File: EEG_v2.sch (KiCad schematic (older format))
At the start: 5 parts, among them P1 CONN_5, P2 CONN_1, P3 CONN_1, P4 USB_A, SW1 SPST

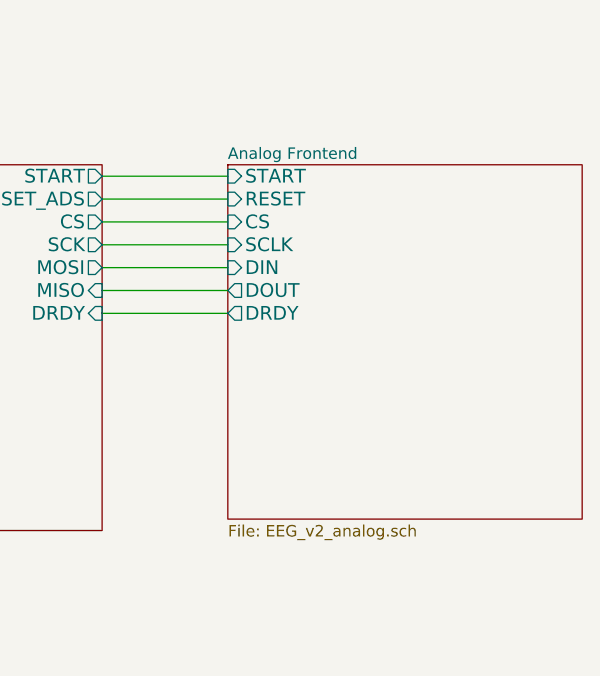
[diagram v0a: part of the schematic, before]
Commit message: Imported sheet pins to main sheet
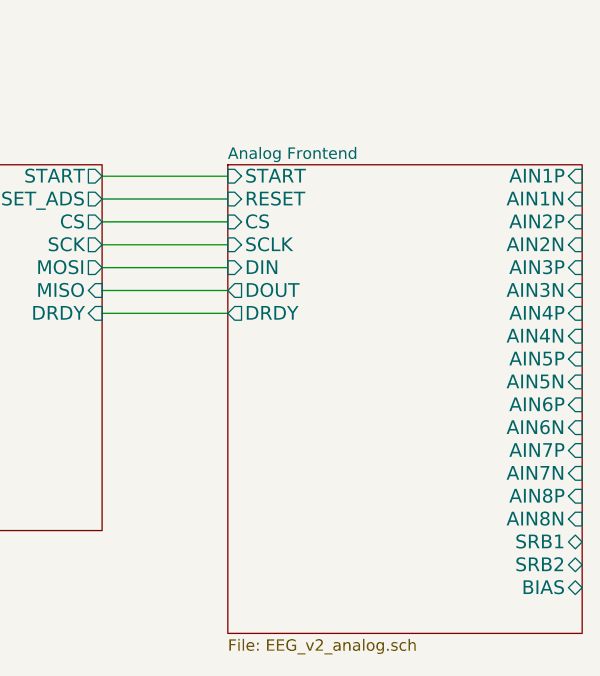
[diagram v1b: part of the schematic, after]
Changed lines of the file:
@@
 $EndDescr
 $Sheet
-S 7000 4200 1550 1550
+S 7000 4200 1550 2050
 U 54B45B18
 F0 "Analog Frontend" 50
@@
 F7 "DOUT" O L 7000 4750 60
 F8 "DRDY" O L 7000 4850 60
+F9 "AIN1P" I R 8550 4250 60
+F10 "AIN1N" I R 8550 4350 60
+F11 "AIN2P" I R 8550 4450 60
+F12 "AIN2N" I R 8550 4550 60
+F13 "AIN3P" I R 8550 4650 60
+F14 "AIN3N" I R 8550 4750 60
+F15 "AIN4P" I R 8550 4850 60
+F16 "AIN4N" I R 8550 4950 60
+F17 "AIN5P" I R 8550 5050 60
+F18 "AIN5N" I R 8550 5150 60
+F19 "AIN6P" I R 8550 5250 60
+F20 "AIN6N" I R 8550 5350 60
+F21 "AIN7P" I R 8550 5450 60
+F22 "AIN7N" I R 8550 5550 60
+F23 "AIN8P" I R 8550 5650 60
+F24 "AIN8N" I R 8550 5750 60
+F25 "SRB1" B R 8550 5850 60
+F26 "SRB2" B R 8550 5950 60
+F27 "BIAS" B R 8550 6050 60
 $EndSheet
 $Sheet

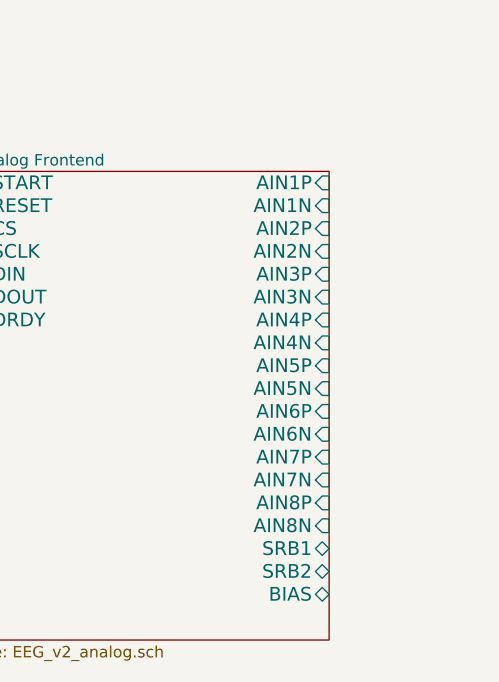
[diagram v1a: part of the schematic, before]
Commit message: Add pin headers for electrodes and debug signals.
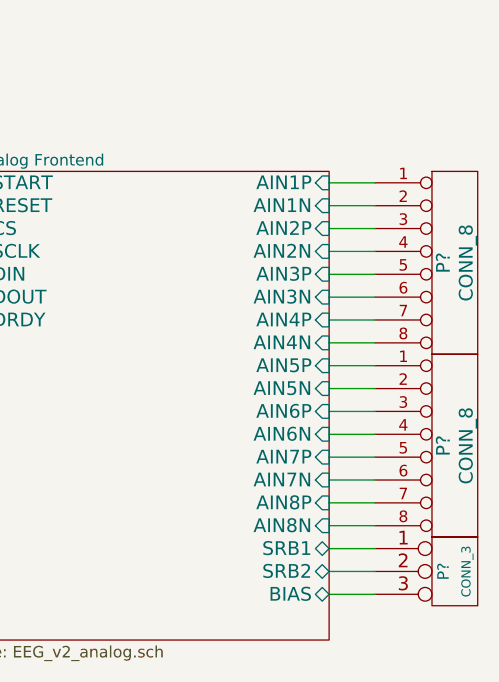
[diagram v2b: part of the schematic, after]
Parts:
- added P? (x2): CONN_8, ~, symbol CONN_8
- added P?: CONN_3, ~, symbol CONN_3
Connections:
- wire segments 26 -> 45
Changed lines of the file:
@@
 Text Notes 1950 6250 0    60   ~ 0
 Note: May change to VIN_RAW instead. Will test first.
+$Comp
+L CONN_8 P?
+U 1 1 54C84F21
+P 9100 4600
+F 0 "P?" V 9050 4600 60  0000 C CNN
+F 1 "CONN_8" V 9150 4600 60  0000 C CNN
+F 2 "~" H 9100 4600 60  0000 C CNN
+F 3 "~" H 9100 4600 60  0000 C CNN
+	1    9100 4600
+	1    0    0    -1
+$EndComp
+$Comp
+L CONN_8 P?
+U 1 1 54C84F2E
+P 9100 5400
+F 0 "P?" V 9050 5400 60  0000 C CNN
+F 1 "CONN_8" V 9150 5400 60  0000 C CNN
+F 2 "~" H 9100 5400 60  0000 C CNN
+F 3 "~" H 9100 5400 60  0000 C CNN
+	1    9100 5400
+	1    0    0    -1
+$EndComp
+$Comp
+L CONN_3 P?
+U 1 1 54C84FBA
+P 9100 5950
+F 0 "P?" V 9050 5950 50  0000 C CNN
+F 1 "CONN_3" V 9150 5950 40  0000 C CNN
+F 2 "~" H 9100 5950 60  0000 C CNN
+F 3 "~" H 9100 5950 60  0000 C CNN
+	1    9100 5950
+	1    0    0    -1
+$EndComp
+Wire Wire Line
+	8550 4250 8750 4250
+Wire Wire Line
+	8750 4350 8550 4350
+Wire Wire Line
+	8550 4450 8750 4450
+Wire Wire Line
+	8750 4550 8550 4550
+Wire Wire Line
+	8550 4650 8750 4650
+Wire Wire Line
+	8750 4750 8550 4750
+Wire Wire Line
+	8550 4850 8750 4850
+Wire Wire Line
+	8750 4950 8550 4950
+Wire Wire Line
+	8550 5050 8750 5050
+Wire Wire Line
+	8750 5150 8550 5150
+Wire Wire Line
+	8550 5250 8750 5250
+Wire Wire Line
+	8750 5350 8550 5350
+Wire Wire Line
+	8550 5450 8750 5450
+Wire Wire Line
+	8750 5550 8550 5550
+Wire Wire Line
+	8550 5650 8750 5650
+Wire Wire Line
+	8750 5750 8550 5750
+Wire Wire Line
+	8550 5850 8750 5850
+Wire Wire Line
+	8750 5950 8550 5950
+Wire Wire Line
+	8550 6050 8750 6050
 $EndSCHEMATC

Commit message: Correct pin headers
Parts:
- removed P1: CONN_5, ~, symbol CONN_5
- added P?: CONN_5X2, ~, symbol CONN_5X2
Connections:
- wire segments 45 -> 54
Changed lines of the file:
@@
 	2650 4750 2750 4750
-Wire Wire Line
-	2750 4750 2750 5400
 Wire Wire Line
 	2650 4850 2750 4850
 Connection ~ 2750 4850
 Wire Wire Line
-	2650 4950 2750 4950
+	2750 4950 2650 4950
 Connection ~ 2750 4950
 $Comp
 L AGND #PWR01
 U 1 1 54C3BF39
-P 3100 5100
-F 0 "#PWR01" H 3100 5100 40  0001 C CNN
-F 1 "AGND" H 3100 5030 50  0000 C CNN
-F 2 "~" H 3100 5100 60  0000 C CNN
-F 3 "~" H 3100 5100 60  0000 C CNN
-	1    3100 5100
-	0    -1   -1   0
+P 2750 5050
+F 0 "#PWR01" H 2750 5050 40  0001 C CNN
+F 1 "AGND" H 2750 4980 50  0000 C CNN
+F 2 "~" H 2750 5050 60  0000 C CNN
+F 3 "~" H 2750 5050 60  0000 C CNN
+	1    2750 5050
+	1    0    0    -1
 $EndComp
 $Comp
@@
 Text Notes 2550 3250 0    60   ~ 0
 BATT_-
-$Comp
-L CONN_5 P1
-U 1 1 54C4DEF5
-P 2200 5600
-F 0 "P1" V 2150 5600 50  0000 C CNN
-F 1 "CONN_5" V 2250 5600 50  0000 C CNN
-F 2 "~" H 2200 5600 60  0000 C CNN
-F 3 "~" H 2200 5600 60  0000 C CNN
-	1    2200 5600
-	-1   0    0    1
-$EndComp
-Wire Wire Line
-	2750 5400 2600 5400
-Wire Wire Line
-	2750 5100 3100 5100
-Connection ~ 2750 5100
-Wire Wire Line
-	2600 5500 4900 5500
-Wire Wire Line
-	2600 5600 4900 5600
-Wire Wire Line
-	4900 5700 2600 5700
-Wire Wire Line
-	2600 5800 2750 5800
-Wire Wire Line
-	2750 5800 2750 6000
+Wire Wire Line
+	2550 5600 4900 5600
+Wire Wire Line
+	4900 5700 3650 5700
 $Comp
 L +3.3V #PWR03
 U 1 1 54C4F12C
-P 2750 6000
-F 0 "#PWR03" H 2750 5960 30  0001 C CNN
-F 1 "+3.3V" H 2750 6110 30  0000 C CNN
-F 2 "~" H 2750 6000 60  0000 C CNN
-F 3 "~" H 2750 6000 60  0000 C CNN
-	1    2750 6000
-	-1   0    0    1
+P 2650 5350
+F 0 "#PWR03" H 2650 5310 30  0001 C CNN
+F 1 "+3.3V" H 2650 5460 30  0000 C CNN
+F 2 "~" H 2650 5350 60  0000 C CNN
+F 3 "~" H 2650 5350 60  0000 C CNN
+	1    2650 5350
+	1    0    0    -1
 $EndComp
 Text Notes 1950 6250 0    60   ~ 0
@@
 Wire Wire Line
 	8550 6050 8750 6050
+$Comp
+L CONN_5X2 P?
+U 1 1 54C8BF12
+P 2150 5700
+F 0 "P?" H 2150 6000 60  0000 C CNN
+F 1 "CONN_5X2" V 2150 5700 50  0000 C CNN
+F 2 "~" H 2150 5700 60  0000 C CNN
+F 3 "~" H 2150 5700 60  0000 C CNN
+	1    2150 5700
+	1    0    0    -1
+$EndComp
+Wire Wire Line
+	2750 4750 2750 5050
+$Comp
+L AGND #PWR?
+U 1 1 54C8DF7C
+P 1450 5500
+F 0 "#PWR?" H 1450 5500 40  0001 C CNN
+F 1 "AGND" H 1450 5430 50  0000 C CNN
+F 2 "~" H 1450 5500 60  0000 C CNN
+F 3 "~" H 1450 5500 60  0000 C CNN
+	1    1450 5500
+	0    1    1    0
+$EndComp
+Wire Wire Line
+	1650 5550 3650 5550
+Wire Wire Line
+	1650 5550 1650 5600
+Wire Wire Line
+	1650 5600 1750 5600
+Wire Wire Line
+	3650 5550 3650 5500
+Wire Wire Line
+	3650 5500 4900 5500
+Wire Wire Line
+	2550 5500 2650 5500
+Wire Wire Line
+	2650 5500 2650 5350
+Wire Wire Line
+	1750 5500 1450 5500
+Wire Wire Line
+	3650 5700 3650 5750
+Wire Wire Line
+	3650 5750 1650 5750
+Wire Wire Line
+	1650 5750 1650 5800
+Wire Wire Line
+	1650 5800 1750 5800
+$Comp
+L +3.3V #PWR?
+U 1 1 54C95C9F
+P 1400 5850
+F 0 "#PWR?" H 1400 5810 30  0001 C CNN
+F 1 "+3.3V" H 1400 5960 30  0000 C CNN
+F 2 "~" H 1400 5850 60  0000 C CNN
+F 3 "~" H 1400 5850 60  0000 C CNN
+	1    1400 5850
+	1    0    0    -1
+$EndComp
+Wire Wire Line
+	1750 5900 1400 5900
+Wire Wire Line
+	1400 5900 1400 5850
 $EndSCHEMATC

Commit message: Modify libraries to be correct. Add pushbuttons and LEDs. Change switch to toggle.
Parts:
- removed SW1: SPST, ~, symbol SPST
- added SW1: SWITCH_INV, ~, symbol SWITCH_INV
- gave numbers to parts that had none: 4
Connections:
- net labels added: VIN_RAW
- net labels removed: +3.3V
- wire segments 54 -> 57
- no-connect marks 0 -> 4
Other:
- moved on the sheet: P2, P3
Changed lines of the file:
@@
 Sheet 1 4
 Title "Project Synapse Prototype Board"
-Date "27 jan 2015"
+Date "28 jan 2015"
 Rev "A.b"
 Comp "Senior Design 14-15"
@@
 	1    0    0    -1
 $EndComp
-$Comp
-L SPST SW1
-U 1 1 54C4411E
-P 3350 2900
-F 0 "SW1" H 3350 3000 70  0000 C CNN
-F 1 "SPST" H 3350 2800 70  0000 C CNN
-F 2 "~" H 3350 2900 60  0000 C CNN
-F 3 "~" H 3350 2900 60  0000 C CNN
-	1    3350 2900
-	1    0    0    -1
-$EndComp
 Wire Wire Line
 	3850 2900 4900 2900
-Wire Wire Line
-	2650 4450 4300 4450
-Wire Wire Line
-	4300 4450 4300 2900
 Connection ~ 4300 2900
 $Comp
 L CONN_1 P2
 U 1 1 54C44DCA
-P 2350 2900
-F 0 "P2" H 2430 2900 40  0000 L CNN
-F 1 "CONN_1" H 2350 2955 30  0001 C CNN
-F 2 "~" H 2350 2900 60  0000 C CNN
-F 3 "~" H 2350 2900 60  0000 C CNN
-	1    2350 2900
+P 1300 2800
+F 0 "P2" H 1380 2800 40  0000 L CNN
+F 1 "CONN_1" H 1300 2855 30  0001 C CNN
+F 2 "~" H 1300 2800 60  0000 C CNN
+F 3 "~" H 1300 2800 60  0000 C CNN
+	1    1300 2800
 	-1   0    0    1
 $EndComp
@@
 L CONN_1 P3
 U 1 1 54C44DD9
-P 2350 3250
-F 0 "P3" H 2430 3250 40  0000 L CNN
-F 1 "CONN_1" H 2350 3305 30  0001 C CNN
-F 2 "~" H 2350 3250 60  0000 C CNN
-F 3 "~" H 2350 3250 60  0000 C CNN
-	1    2350 3250
+P 1350 3400
+F 0 "P3" H 1430 3400 40  0000 L CNN
+F 1 "CONN_1" H 1350 3455 30  0001 C CNN
+F 2 "~" H 1350 3400 60  0000 C CNN
+F 3 "~" H 1350 3400 60  0000 C CNN
+	1    1350 3400
 	-1   0    0    1
 $EndComp
 Wire Wire Line
-	2500 2900 2850 2900
-Wire Wire Line
-	2500 3250 2750 3250
-Wire Wire Line
-	2750 3250 2750 3350
+	1450 2800 2850 2800
+Wire Wire Line
+	1500 3400 1750 3400
+Wire Wire Line
+	1750 3400 1750 3500
 $Comp
 L AGND #PWR02
 U 1 1 54C45735
-P 2750 3350
-F 0 "#PWR02" H 2750 3350 40  0001 C CNN
-F 1 "AGND" H 2750 3280 50  0000 C CNN
-F 2 "~" H 2750 3350 60  0000 C CNN
-F 3 "~" H 2750 3350 60  0000 C CNN
-	1    2750 3350
-	1    0    0    -1
-$EndComp
-Text Label 2550 2900 0    60   ~ 0
+P 1750 3500
+F 0 "#PWR02" H 1750 3500 40  0001 C CNN
+F 1 "AGND" H 1750 3430 50  0000 C CNN
+F 2 "~" H 1750 3500 60  0000 C CNN
+F 3 "~" H 1750 3500 60  0000 C CNN
+	1    1750 3500
+	1    0    0    -1
+$EndComp
+Text Label 2550 2800 0    60   ~ 0
 BATT_+
-Text Notes 2550 3250 0    60   ~ 0
+Text Notes 1550 3400 0    60   ~ 0
 BATT_-
 Wire Wire Line
@@
 Wire Wire Line
 	4900 5700 3650 5700
-$Comp
-L +3.3V #PWR03
-U 1 1 54C4F12C
-P 2650 5350
-F 0 "#PWR03" H 2650 5310 30  0001 C CNN
-F 1 "+3.3V" H 2650 5460 30  0000 C CNN
-F 2 "~" H 2650 5350 60  0000 C CNN
-F 3 "~" H 2650 5350 60  0000 C CNN
-	1    2650 5350
-	1    0    0    -1
-$EndComp
 Text Notes 1950 6250 0    60   ~ 0
 Note: May change to VIN_RAW instead. Will test first.
 $Comp
-L CONN_8 P?
+L CONN_8 P5
 U 1 1 54C84F21
 P 9100 4600
-F 0 "P?" V 9050 4600 60  0000 C CNN
+F 0 "P5" V 9050 4600 60  0000 C CNN
 F 1 "CONN_8" V 9150 4600 60  0000 C CNN
 F 2 "~" H 9100 4600 60  0000 C CNN
@@
 $EndComp
 $Comp
-L CONN_8 P?
+L CONN_8 P6
 U 1 1 54C84F2E
 P 9100 5400
-F 0 "P?" V 9050 5400 60  0000 C CNN
+F 0 "P6" V 9050 5400 60  0000 C CNN
 F 1 "CONN_8" V 9150 5400 60  0000 C CNN
 F 2 "~" H 9100 5400 60  0000 C CNN
@@
 $EndComp
 $Comp
-L CONN_3 P?
+L CONN_3 P7
 U 1 1 54C84FBA
 P 9100 5950
-F 0 "P?" V 9050 5950 50  0000 C CNN
+F 0 "P7" V 9050 5950 50  0000 C CNN
 F 1 "CONN_3" V 9150 5950 40  0000 C CNN
 F 2 "~" H 9100 5950 60  0000 C CNN
@@
 	8550 6050 8750 6050
 $Comp
-L CONN_5X2 P?
+L CONN_5X2 P1
 U 1 1 54C8BF12
 P 2150 5700
-F 0 "P?" H 2150 6000 60  0000 C CNN
+F 0 "P1" H 2150 6000 60  0000 C CNN
 F 1 "CONN_5X2" V 2150 5700 50  0000 C CNN
 F 2 "~" H 2150 5700 60  0000 C CNN
@@
 	2750 4750 2750 5050
 $Comp
-L AGND #PWR?
+L AGND #PWR03
 U 1 1 54C8DF7C
 P 1450 5500
-F 0 "#PWR?" H 1450 5500 40  0001 C CNN
+F 0 "#PWR03" H 1450 5500 40  0001 C CNN
 F 1 "AGND" H 1450 5430 50  0000 C CNN
 F 2 "~" H 1450 5500 60  0000 C CNN
@@
 	3650 5500 4900 5500
 Wire Wire Line
-	2550 5500 2650 5500
-Wire Wire Line
-	2650 5500 2650 5350
+	2650 5500 2550 5500
+Wire Wire Line
+	2650 5250 2650 5500
 Wire Wire Line
 	1750 5500 1450 5500
@@
 Wire Wire Line
 	1650 5800 1750 5800
-$Comp
-L +3.3V #PWR?
-U 1 1 54C95C9F
-P 1400 5850
-F 0 "#PWR?" H 1400 5810 30  0001 C CNN
-F 1 "+3.3V" H 1400 5960 30  0000 C CNN
-F 2 "~" H 1400 5850 60  0000 C CNN
-F 3 "~" H 1400 5850 60  0000 C CNN
-	1    1400 5850
-	1    0    0    -1
-$EndComp
-Wire Wire Line
-	1750 5900 1400 5900
-Wire Wire Line
-	1400 5900 1400 5850
+Wire Wire Line
+	1300 5900 1750 5900
+NoConn ~ 2550 5700
+NoConn ~ 2550 5800
+NoConn ~ 2550 5900
+NoConn ~ 1750 5700
+Text GLabel 4300 2700 1    60   Input ~ 0
+VIN_RAW
+Text GLabel 1200 5250 0    60   Input ~ 0
+VIN_RAW
+Wire Wire Line
+	1300 5900 1300 5250
+Wire Wire Line
+	1200 5250 2650 5250
+Connection ~ 1300 5250
+Wire Wire Line
+	4300 2700 4300 2900
+Wire Wire Line
+	2650 4450 2750 4450
+Wire Wire Line
+	2750 4450 2750 3000
+Wire Wire Line
+	2750 3000 2850 3000
+$Comp
+L SWITCH_INV SW1
+U 1 1 54CBF41B
+P 3350 2900
+F 0 "SW1" H 3150 3050 50  0000 C CNN
+F 1 "SWITCH_INV" H 3200 2750 50  0000 C CNN
+F 2 "~" H 3350 2900 60  0000 C CNN
+F 3 "~" H 3350 2900 60  0000 C CNN
+	1    3350 2900
+	-1   0    0    1
+$EndComp
 $EndSCHEMATC

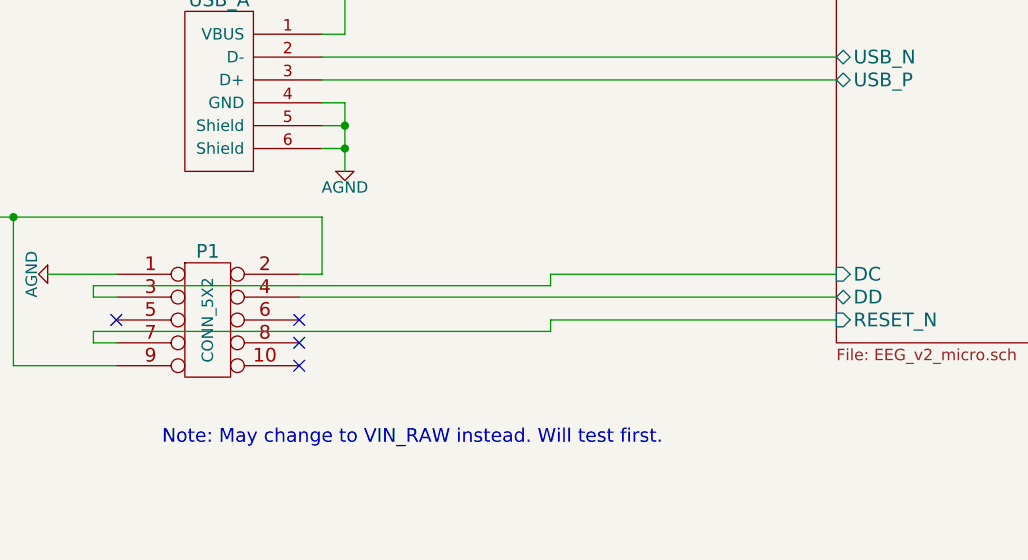
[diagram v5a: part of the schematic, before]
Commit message: Add reset button / jumper
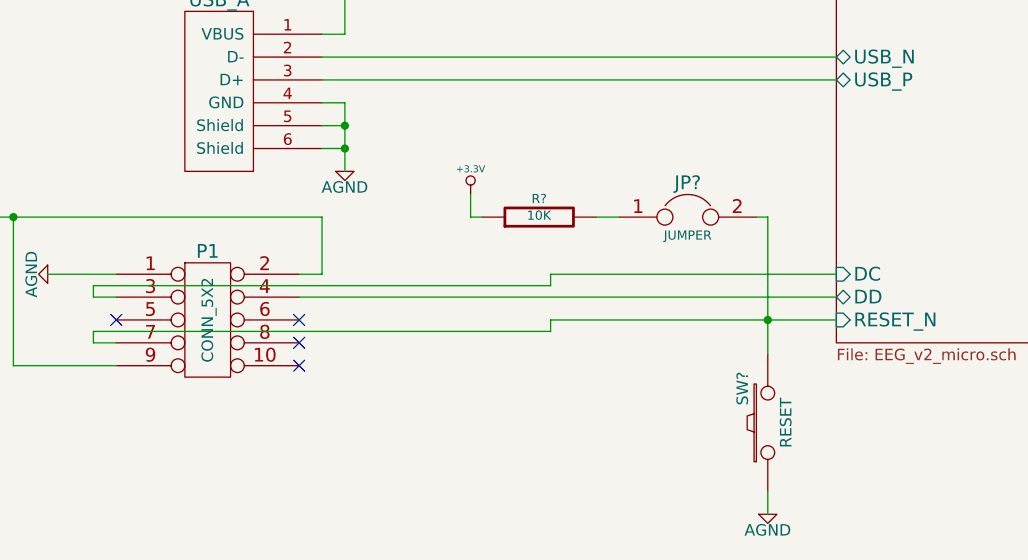
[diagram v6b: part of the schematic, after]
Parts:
- added JP?: JUMPER, ~, symbol JUMPER
- added R?: 10K, ~, symbol R
- added SW?: RESET, ~, symbol SW_PUSH
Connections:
- net AGND: now also SW?.1
- net Microcontroller/RESET_N: now also JP?.2, SW?.2
- new net: JP?.1, R?.2
- new net +3.3V: R?.1
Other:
- note removed: "Note: May change to VIN_RAW instead. Will test first."
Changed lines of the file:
@@
 Wire Wire Line
 	2550 5600 4900 5600
-Wire Wire Line
-	4900 5700 3650 5700
-Text Notes 1950 6250 0    60   ~ 0
-Note: May change to VIN_RAW instead. Will test first.
 $Comp
 L CONN_8 P5
@@
 	-1   0    0    1
 $EndComp
+$Comp
+L R R?
+U 1 1 54CA2962
+P 3600 5250
+F 0 "R?" V 3680 5250 40  0000 C CNN
+F 1 "10K" V 3607 5251 40  0000 C CNN
+F 2 "~" V 3530 5250 30  0000 C CNN
+F 3 "~" H 3600 5250 30  0000 C CNN
+	1    3600 5250
+	0    -1   -1   0
+$EndComp
+$Comp
+L +3.3V #PWR?
+U 1 1 54CA3BAD
+P 3300 5150
+F 0 "#PWR?" H 3300 5110 30  0001 C CNN
+F 1 "+3.3V" H 3300 5260 30  0000 C CNN
+F 2 "~" H 3300 5150 60  0000 C CNN
+F 3 "~" H 3300 5150 60  0000 C CNN
+	1    3300 5150
+	1    0    0    -1
+$EndComp
+Wire Wire Line
+	4600 5250 4600 5850
+Connection ~ 4600 5700
+Wire Wire Line
+	3650 5700 4900 5700
+$Comp
+L JUMPER JP?
+U 1 1 54CAAA23
+P 4250 5250
+F 0 "JP?" H 4250 5400 60  0000 C CNN
+F 1 "JUMPER" H 4250 5170 40  0000 C CNN
+F 2 "~" H 4250 5250 60  0000 C CNN
+F 3 "~" H 4250 5250 60  0000 C CNN
+	1    4250 5250
+	1    0    0    -1
+$EndComp
+Wire Wire Line
+	3300 5150 3300 5250
+Wire Wire Line
+	3300 5250 3350 5250
+Wire Wire Line
+	4600 5250 4550 5250
+Wire Wire Line
+	3950 5250 3850 5250
+$Comp
+L SW_PUSH SW?
+U 1 1 54CABD6B
+P 4600 6150
+F 0 "SW?" H 4750 6260 50  0000 C CNN
+F 1 "RESET" H 4600 6070 50  0000 C CNN
+F 2 "~" H 4600 6150 60  0000 C CNN
+F 3 "~" H 4600 6150 60  0000 C CNN
+	1    4600 6150
+	0    -1   -1   0
+$EndComp
+$Comp
+L AGND #PWR?
+U 1 1 54CAD291
+P 4600 6550
+F 0 "#PWR?" H 4600 6550 40  0001 C CNN
+F 1 "AGND" H 4600 6480 50  0000 C CNN
+F 2 "~" H 4600 6550 60  0000 C CNN
+F 3 "~" H 4600 6550 60  0000 C CNN
+	1    4600 6550
+	1    0    0    -1
+$EndComp
+Wire Wire Line
+	4600 6450 4600 6550
 $EndSCHEMATC

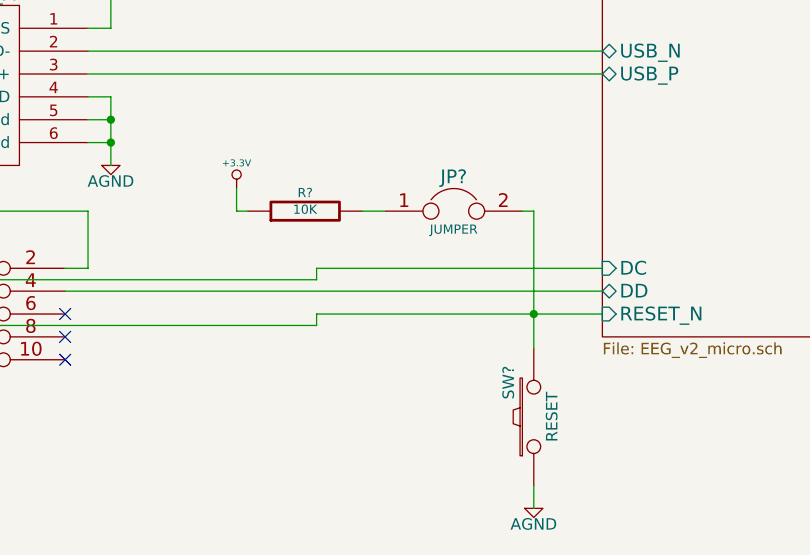
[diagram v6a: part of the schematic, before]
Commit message: Add footprints
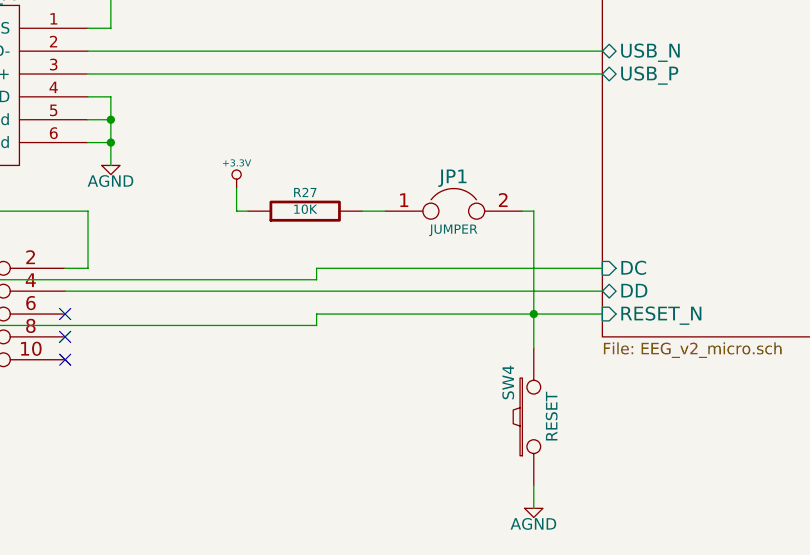
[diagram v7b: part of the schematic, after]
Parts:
- gave numbers to parts that had none: 3
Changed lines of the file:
@@
 $EndComp
 $Comp
-L R R?
+L R R27
 U 1 1 54CA2962
 P 3600 5250
-F 0 "R?" V 3680 5250 40  0000 C CNN
+F 0 "R27" V 3680 5250 40  0000 C CNN
 F 1 "10K" V 3607 5251 40  0000 C CNN
 F 2 "~" V 3530 5250 30  0000 C CNN
@@
 $EndComp
 $Comp
-L +3.3V #PWR?
+L +3.3V #PWR04
 U 1 1 54CA3BAD
 P 3300 5150
-F 0 "#PWR?" H 3300 5110 30  0001 C CNN
+F 0 "#PWR04" H 3300 5110 30  0001 C CNN
 F 1 "+3.3V" H 3300 5260 30  0000 C CNN
 F 2 "~" H 3300 5150 60  0000 C CNN
@@
 	3650 5700 4900 5700
 $Comp
-L JUMPER JP?
+L JUMPER JP1
 U 1 1 54CAAA23
 P 4250 5250
-F 0 "JP?" H 4250 5400 60  0000 C CNN
+F 0 "JP1" H 4250 5400 60  0000 C CNN
 F 1 "JUMPER" H 4250 5170 40  0000 C CNN
 F 2 "~" H 4250 5250 60  0000 C CNN
@@
 	3950 5250 3850 5250
 $Comp
-L SW_PUSH SW?
+L SW_PUSH SW4
 U 1 1 54CABD6B
 P 4600 6150
-F 0 "SW?" H 4750 6260 50  0000 C CNN
+F 0 "SW4" H 4750 6260 50  0000 C CNN
 F 1 "RESET" H 4600 6070 50  0000 C CNN
 F 2 "~" H 4600 6150 60  0000 C CNN
@@
 $EndComp
 $Comp
-L AGND #PWR?
+L AGND #PWR05
 U 1 1 54CAD291
 P 4600 6550
-F 0 "#PWR?" H 4600 6550 40  0001 C CNN
+F 0 "#PWR05" H 4600 6550 40  0001 C CNN
 F 1 "AGND" H 4600 6480 50  0000 C CNN
 F 2 "~" H 4600 6550 60  0000 C CNN
